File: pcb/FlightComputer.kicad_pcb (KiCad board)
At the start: 2 copper layers, 23 x 50.2 mm, 74 parts, among them J1 USB4105-GF-A, Q1 DMG3415U, Q2 Si2302CDS, Q3 Si2302CDS, SW1 RESET, SW2 BOOT, U2 ICM-42670-P, U3 ESP32-C3-MINI-1, U5 SY8088, U6 MCP73831T-2ACI/OT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

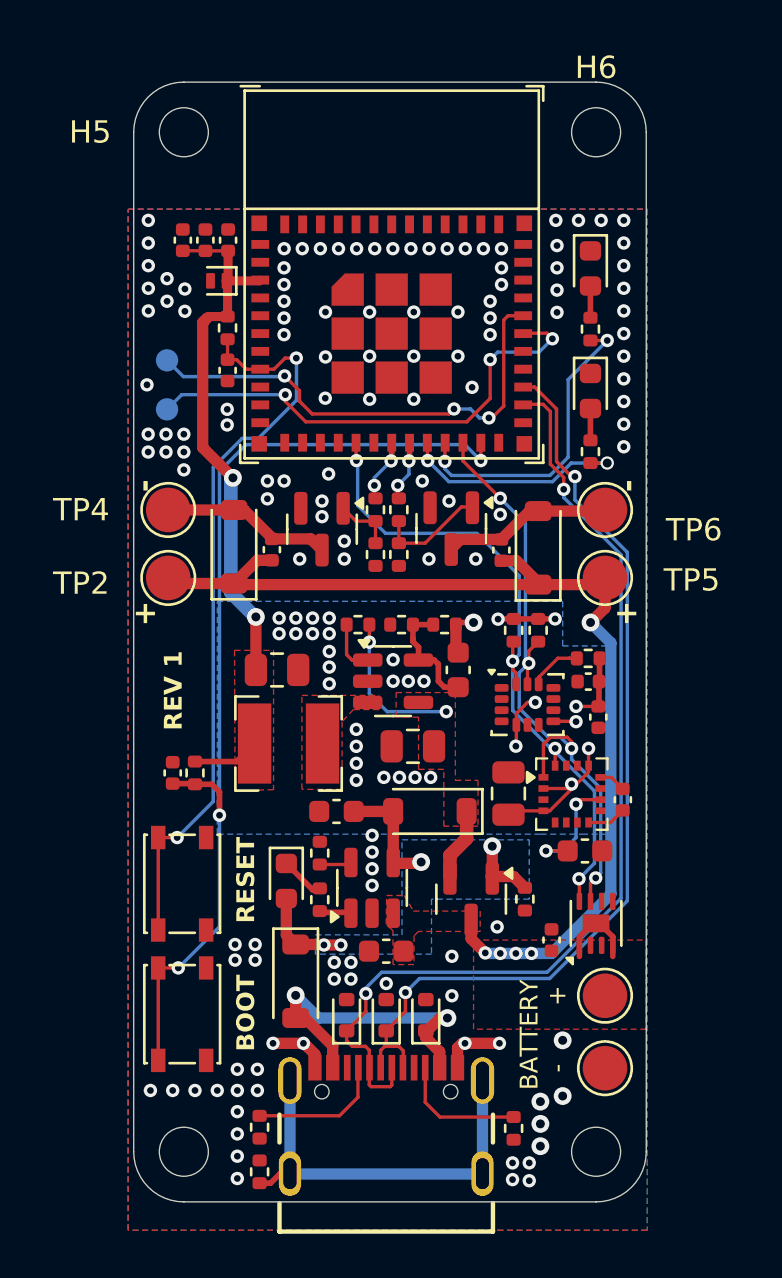
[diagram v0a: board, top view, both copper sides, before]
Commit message: Connect IO0 to IMU interrupt
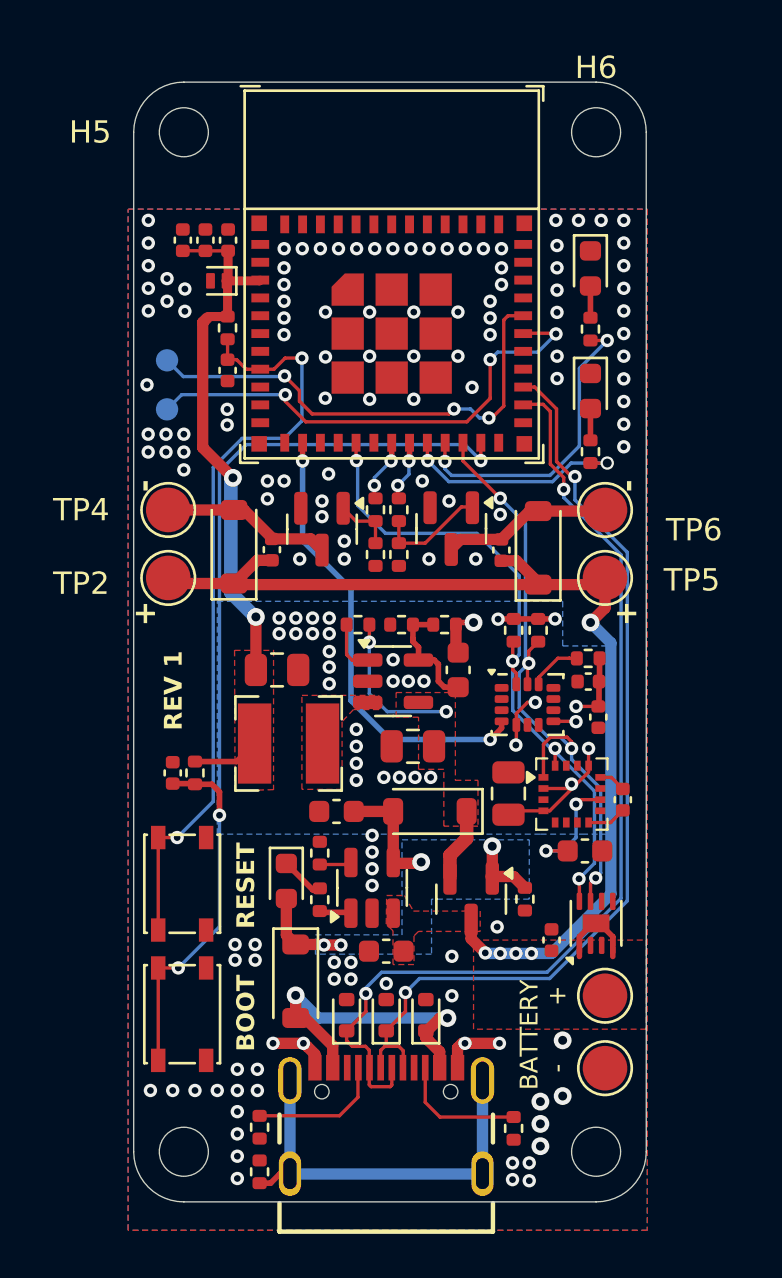
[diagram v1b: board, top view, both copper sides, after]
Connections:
- U2 pad 4: unconnected-(U2-INT1/INT-Pad4) -> IO13
- U3 pad 13: unconnected-(U3-GPIO1/ADC1_CH1/XTAL_32K_N-Pad13) -> IO13
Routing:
- net IO13: track 0.00 -> 20.5 mm, vias 0 -> 2
- net CHIP_PU: track 33.5 -> 34.6 mm
- net GND: vias 150 -> 152

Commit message: Hide labels
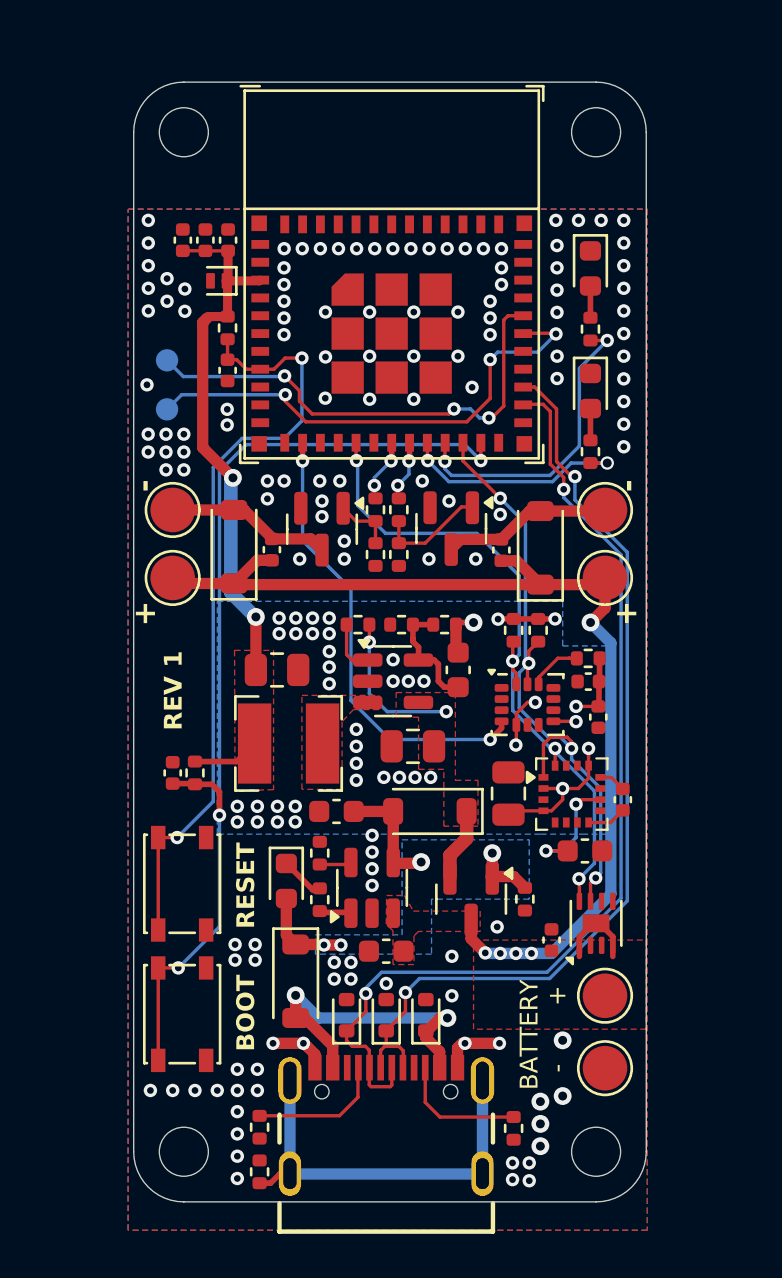
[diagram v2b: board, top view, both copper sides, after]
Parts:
- moved TP2 0.20 mm to (138.5, 99.2)
- moved TP4 0.20 mm to (138.5, 96.2)
- moved D11 0.10 mm to (155.0, 97.9)
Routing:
- net GND: vias 152 -> 162

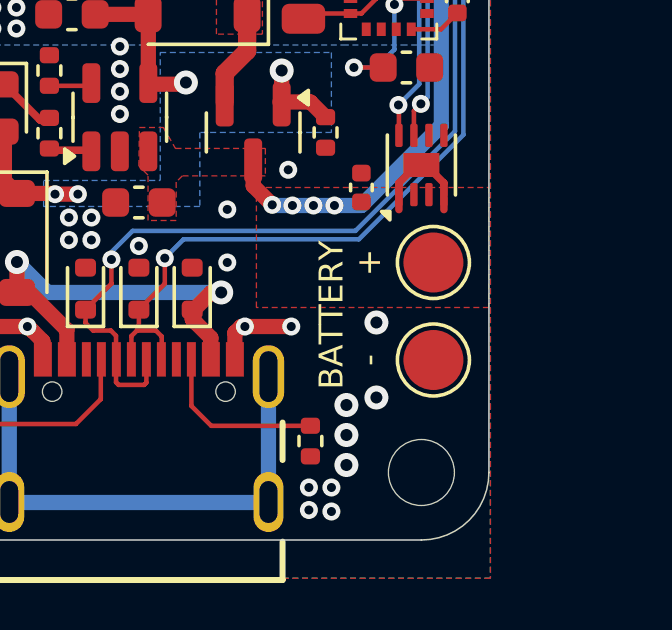
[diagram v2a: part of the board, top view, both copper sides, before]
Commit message: Add GND vias, clean up schematic
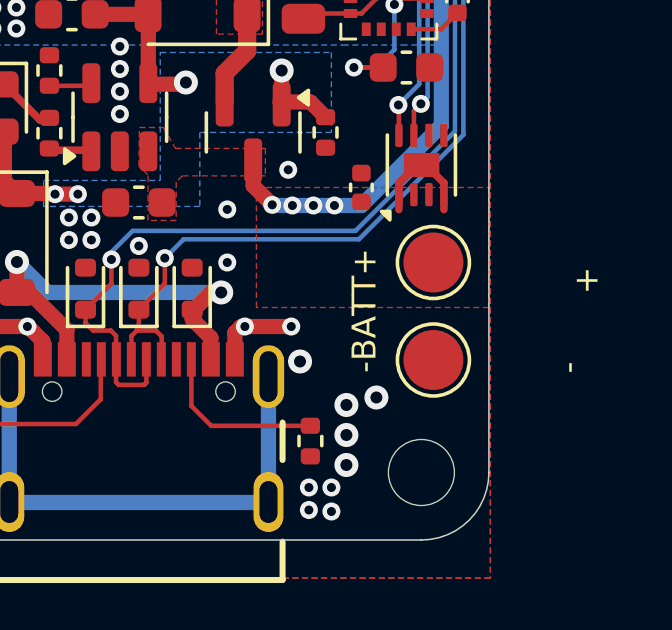
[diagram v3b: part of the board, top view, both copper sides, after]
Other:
- board text added: "-BATT+"
- board text removed: "BATTERY"
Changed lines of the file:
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@@
 	)
 	(gr_text "+"
-		(at 155.75 118 90)
+		(at 163 118.6 90)
 		(layer "F.SilkS")
 		(effects
@@
 	)
 	(gr_text "-"
-		(at 155.75 121.25 90)
+		(at 162.4 121.5 90)
 		(layer "F.SilkS" knockout)
 		(effects
@@
 		)
 	)
-	(gr_text "BATTERY"
-		(at 154.5 119.75 90)
+	(gr_text "-BATT+"
+		(at 155.6 119.6 90)
 		(layer "F.SilkS" knockout)
 		(effects
@@
 	)
 	(via
-		(at 156 120)
+		(at 153.454 121.3)
 		(size 0.8)
 		(drill 0.4)
